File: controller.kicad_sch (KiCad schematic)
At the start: 39 parts, among them U3 STM32F767ZITx, Y1 Crystal

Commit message: Added ESD, updated Footprints, BOM, etc.
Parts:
- removed JP1: SolderJumper_3_Bridged, Jumper:SolderJumper-3_P1.3mm_Bridged12_Pad1.0x1.5mm, symbol Jumper:SolderJumper_3_Bridged12
- removed TP1: UART_RTS, TestPoint:TestPoint_Pad_D1.5mm, symbol Connector:TestPoint
- removed TP1: UART_CTS, TestPoint:TestPoint_Pad_D1.5mm, symbol Connector:TestPoint
- removed Y1: Crystal, TimosFootprints:Crystal_SMD_MicroCrystal_CC6F_T1F_128, symbol Device:Crystal
- added C37, C38: C, Capacitor_SMD:C_0201_0603Metric, symbol Device:C
- added R56: 0R, Resistor_SMD:R_0201_0603Metric, symbol Device:R
- added Y1: CX2016SA25000F0FRZC1, TimosFootprints:CX2016SA25000F0FRZC1, symbol Device:Crystal_GND24
- C3: value 0.1u -> 100n
- D1: value OPTION_LED_1 -> SML-LX0402USBC-TR
- D1: value OPTION_LED_2 -> SML-LX0402USBC-TR
- SW_RESET: value SW_Push -> PTS645SM43SMTR92 LFS
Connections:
- net +3.3V: now also R30.1, R31.1; no longer R30.2, R31.2
- net GEN_SPI_CLK: now also U3.69 (PB10); no longer U3.126 (PG11)
- net GEN_SPI_CSEL: now also U3.28 (PC2); no longer U3.128 (PG13)
- net GEN_SPI_DATA: now also U3.27 (PC1)
- net GND: now also C37.2, C38.2, Y1.2, Y1.4
- net GPIO_BTN_1: now also U3.128 (PG13); no longer U3.90 (PG5)
- net GPIO_BTN_2: now also U3.127 (PG12); no longer U3.89 (PG4)
- net GPIO_LED_1: now also U3.126 (PG11); no longer U3.88 (PG3)
- net GPIO_LED_2: now also U3.125 (PG10); no longer U3.87 (PG2)
- net GPIO_LED_2_JUNCTION: now reaches D1.2 (A), R11.1
- net MCU_VDDUSB: now reaches U3.95 (VDDUSB)
- net MCU_VDDUSB: now also R31.2; no longer R31.1
- net GPIO_LED_1_JUNCTION: now reaches D1.2 (A), R11.1
- net MCU_PDR_ON: now reaches R29.2, U3.143 (PDR_ON)
- net MCU_VDDSDMMC: now reaches U3.121 (VDDSDMMC)
- net MCU_VDDSDMMC: now also R30.2; no longer R30.1
- net JTAG_TMS: now reaches U3.105 (PA13)
- net JTAG_TCK: now reaches U3.109 (PA14)
- net JTAG_TDI: now reaches U3.110 (PA15)
- net JTAG_TDO: now reaches U3.133 (PB3)
- net JTAG_NTRST: now reaches U3.134 (PB4)
- net MCU_BOOT0: now reaches R27.1, SW_BOOT1.2, U3.138 (BOOT0)
- net MCU_VBAT: now reaches R12.2, U3.6 (VBAT)
- net CRYSTAL_PH0 renamed MCU_CRYSTAL_PH0
- net MCU_CRYSTAL_PH0: now also C38.1, Y1.1
- net CRYSTAL_PH1 renamed MCU_CRYSTAL_PH1
- net MCU_CRYSTAL_PH1: now also R56.2
- net GEN_SPI_DATA_MCU_0: no longer names the net of U3.43 (PA7)
- net GEN_SPI_DATA_MCU_1: no longer names the net of U3.135 (PB5)
- net GLOBAL_NRESET renamed JTAG_NSRST
- new net MCU_CRYSTAL_3: C37.1, R56.1, Y1.3
- no-connect marks 93 -> 89
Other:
- note added: "TODO: Cs + R dimensionieren"
- note added: "TODO: Schalter heraussuchen"
- note removed: "If there is a problem with a timer and an SPI output pin, use this jumper to select the correct SPI output on the MCU."
- note removed: "Sine Generator SPI Data selection"
- note removed: "TODO"
- moved on the sheet: C3, D1, R11, R12, R27, R29, R30, R31, SW_BOOT1, SW_RESET, U3

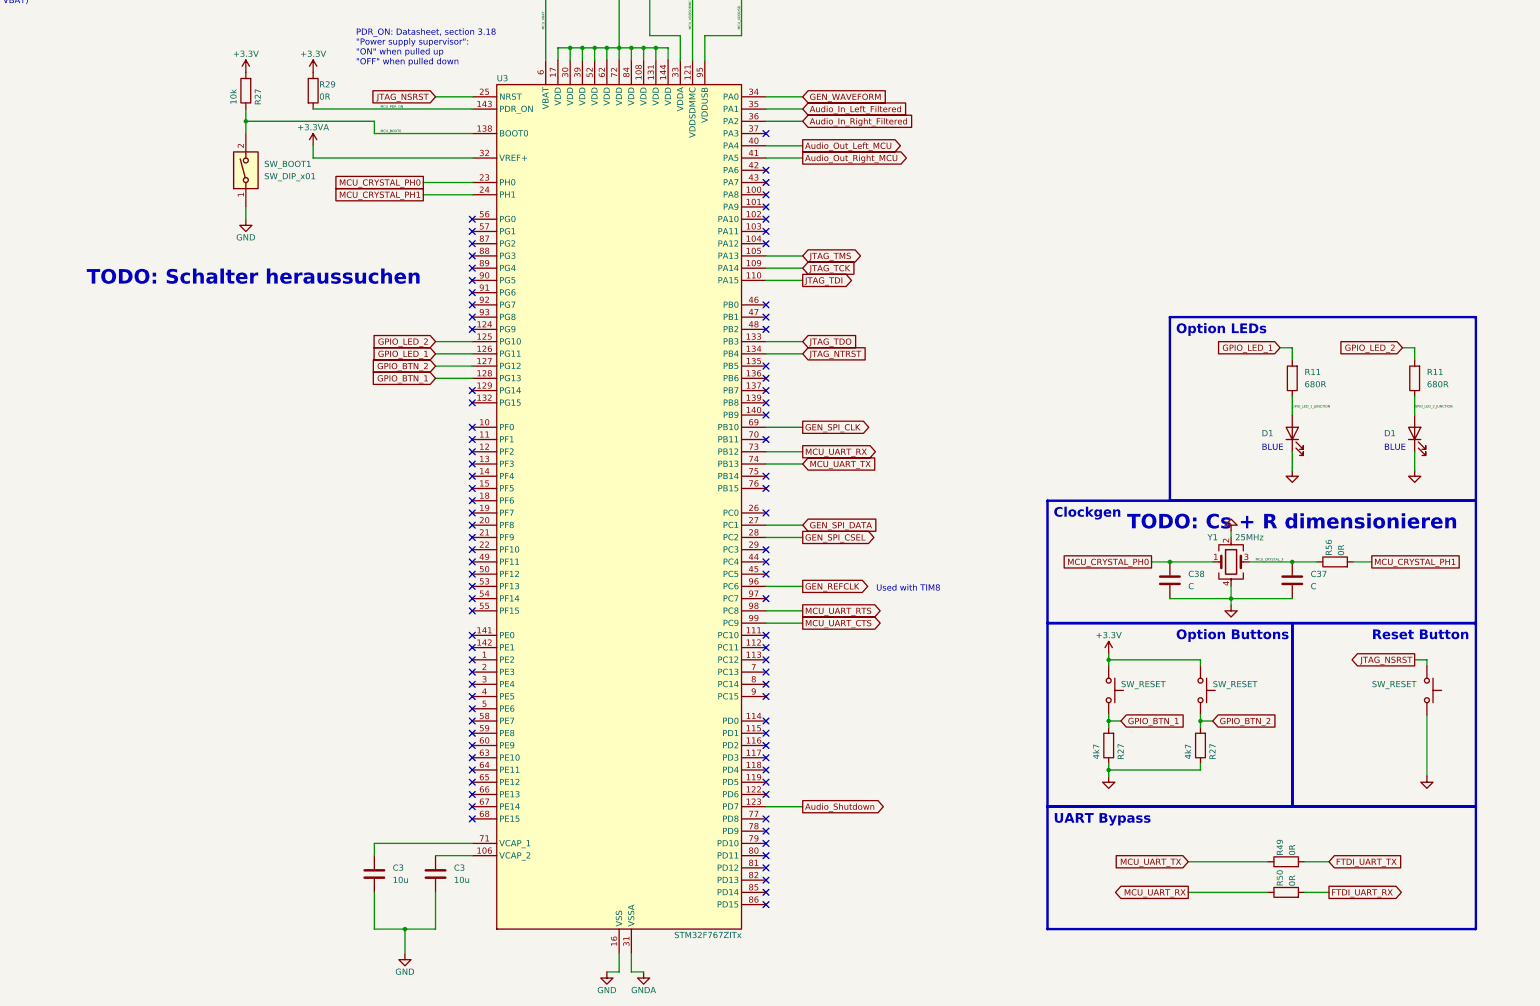
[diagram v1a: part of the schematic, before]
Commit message: Schematic is done for now, starting layout
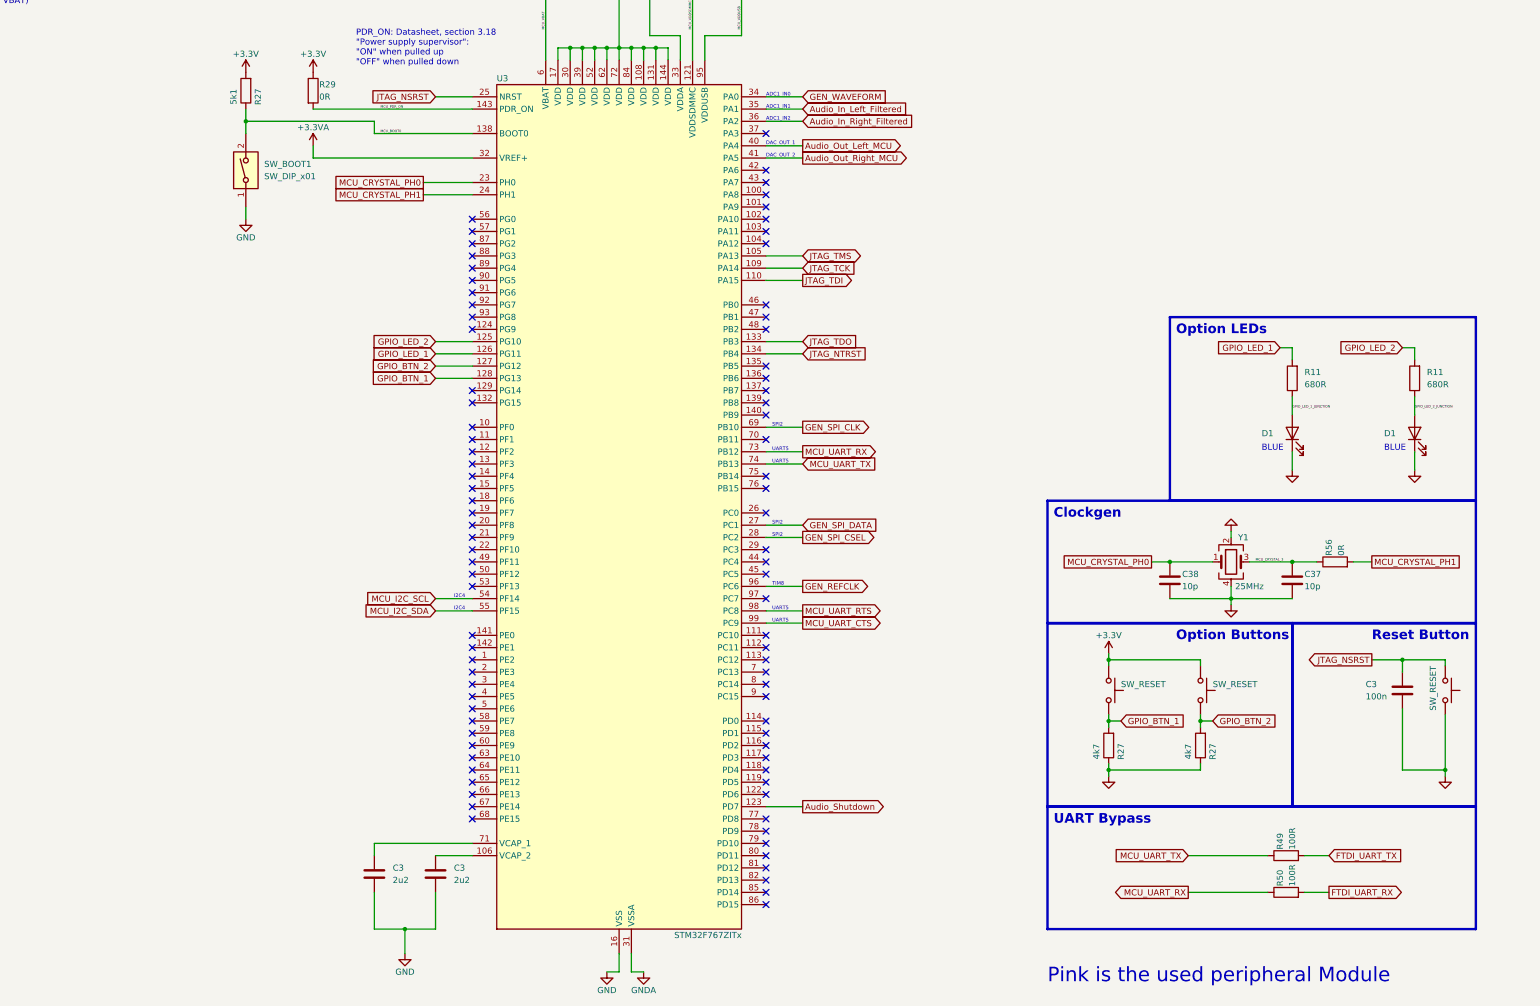
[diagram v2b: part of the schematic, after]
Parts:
- added C3: 100n, Capacitor_SMD:C_0603_1608Metric, symbol Device:C
- C3: value 10u -> 2u2
- C37, C38: value C -> 10p
- D1: Distributor Link (none) -> https://www.mouser.de/ProductDetail/Lumex/SML-LX0402USBC-TR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; MFN SML-LX0402USBC-TR -> (none); Manufacturer (none) -> Lumex; Manufacturer Number (none) -> SML-LX0402USBC-TR
- R27: value 10k -> 5k1
- R49, R50: value 0R -> 100R
- SW_BOOT1: footprint Button_Switch_THT:SW_DIP_SPSTx01_Slide_9.78x4.72mm_W7.62mm_P2.54mm -> TimosFootprints:DS01-254-L-01BE; Distributor Link (none) -> https://www.mouser.de/ProductDetail/CUI-Devices/DS01-254-L-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; Manufacturer (none) -> CUI Devices; Manufacturer Number (none) -> DS01-254-L-01BE
- SW_RESET: Distributor Link (none) -> https://www.mouser.de/ProductDetail/CK/PTS645SM43SMTR92LFS?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; MFN PTS645SM43SMTR92 LFS -> (none); Manufacturer (none) -> C&K; Manufacturer Number (none) -> PTS645SM43SMTR92 LFS
- U3: Distributor Link (none) -> https://www.mouser.de/ProductDetail/STMicroelectronics/STM3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; Manufacturer (none) -> STMicroelectronics; Manufacturer Number (none) -> STM32F767ZIT6
- Y1: value CX2016SA25000F0FRZC1 -> 25MHz; footprint TimosFootprints:CX2016SA25000F0FRZC1 -> Crystal:Crystal_SMD_2016-4Pin_2.0x1.6mm; Distributor Link (none) -> https://www.mouser.de/ProductDetail/KYOCERA-AVX/CX2016SA250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; Frequenz 25MHz -> (none); MFN CX2016SA25000F0FRZC1 -> (none); Manufacturer (none) -> KYOCERA AVX; Manufacturer Number (none) -> CX2016SA25000F0FRZC1
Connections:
- net GND: now also C3.2
- net JTAG_NSRST: now also C3.1
- net MCU_I2C_SCL: now reaches U3.54 (PF14)
- net MCU_I2C_SDA: now reaches U3.55 (PF15)
- no-connect marks 89 -> 87
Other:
- note added: "ADC1_IN0"
- note added: "ADC1_IN1"
- note added: "ADC1_IN2"
- note added: "DAC_OUT_1"
- note added: "DAC_OUT_2"
- note added: "I2C4"
- note added: "Pink is the used peripheral Module"
- note added: "SPI2"
- note added: "TIM8"
- note added: "UART5"
- note removed: "TODO: Cs + R dimensionieren"
- note removed: "TODO: Schalter heraussuchen"
- note removed: "Used with TIM8"
- moved on the sheet: R49, SW_RESET

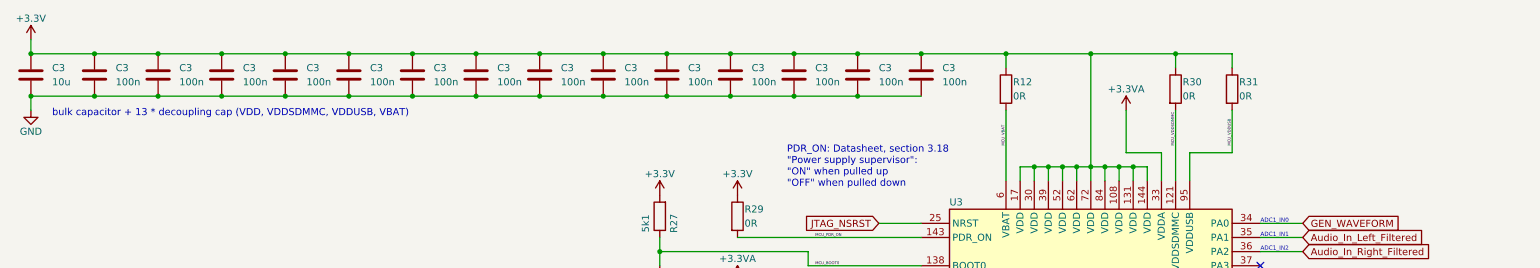
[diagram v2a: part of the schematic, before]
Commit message: Layout done, footprints mostly assigned, 3D models assigned if not annoying to get. Few TODOs left and they are marked on the PCB.
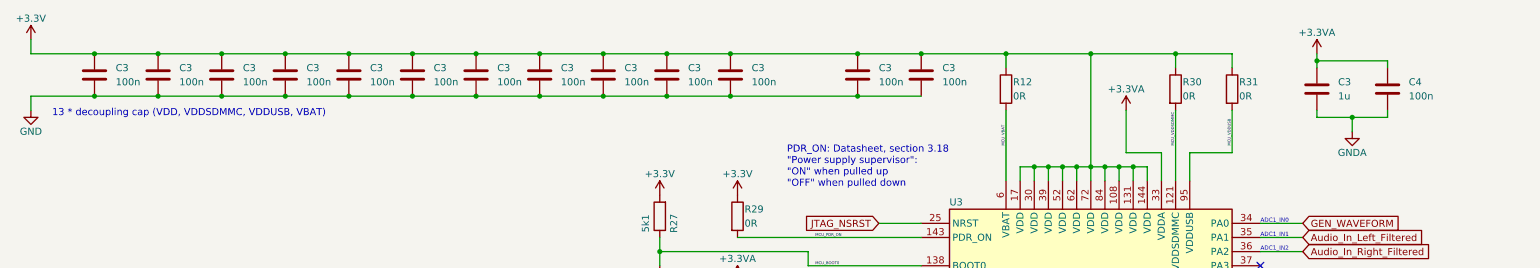
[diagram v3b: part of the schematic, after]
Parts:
- removed C3: 10u, Capacitor_SMD:C_0603_1608Metric, symbol Device:C
- removed C3: 100n, Capacitor_SMD:C_0603_1608Metric, symbol Device:C
- added C3: 1u, Capacitor_SMD:C_0603_1608Metric, symbol Device:C
- added C4: 100n, Capacitor_SMD:C_0603_1608Metric, symbol Device:C
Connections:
- net +3.3VA: now also C3.1, C4.1
- net GNDA: now also C3.2, C4.2
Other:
- note added: "13 * decoupling cap (VDD, VDDSDMMC, VDDUSB, VBAT)"
- note removed: "bulk capacitor + 13 * decoupling cap (VDD, VDDSDMMC, VDDUSB, VBAT)"

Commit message: Board outline finished, component placement, added markers, added annotations, etc.
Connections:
- net GPIO_OPT_0: now reaches U3.65 (PE12)
- net GPIO_OPT_1: now reaches U3.66 (PE13)
- net GPIO_OPT_2: now reaches U3.67 (PE14)
- net GPIO_OPT_3: now reaches U3.68 (PE15)
- no-connect marks 87 -> 83
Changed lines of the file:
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@@
   )
   (no_connect (at 185.42 157.48))
-  (no_connect (at 185.42 210.82))
   (no_connect (at 185.42 167.64))
   (no_connect (at 246.38 218.44))
@@
   (no_connect (at 246.38 127))
   (no_connect (at 185.42 170.18))
-  (no_connect (at 185.42 218.44))
   (no_connect (at 246.38 205.74))
   (no_connect (at 185.42 195.58))
@@
   (no_connect (at 246.38 180.34))
   (no_connect (at 246.38 165.1))
-  (no_connect (at 185.42 215.9))
   (no_connect (at 185.42 193.04))
   (no_connect (at 246.38 220.98))
@@
   (no_connect (at 246.38 124.46))
   (no_connect (at 246.38 200.66))
-  (no_connect (at 185.42 213.36))
   (no_connect (at 185.42 185.42))
   (no_connect (at 246.38 132.08))
@@
     (stroke (width 0) (type default))
   )
+  (wire (pts (xy 177.8 215.9) (xy 185.42 215.9))
+    (stroke (width 0) (type default))
+  )
   (wire (pts (xy 246.38 144.78) (xy 254 144.78))
     (stroke (width 0) (type default))
@@
     (stroke (width 0) (type default))
   )
+  (wire (pts (xy 177.8 210.82) (xy 185.42 210.82))
+    (stroke (width 0) (type default))
+  )
   (wire (pts (xy 246.38 160.02) (xy 254 160.02))
     (stroke (width 0) (type default))
@@
     (stroke (width 0) (type default))
   )
+  (wire (pts (xy 177.8 213.36) (xy 185.42 213.36))
+    (stroke (width 0) (type default))
+  )
   (wire (pts (xy 233.68 55.88) (xy 233.68 60.96))
     (stroke (width 0) (type default))
@@
   )
   (wire (pts (xy 205.74 58.42) (xy 205.74 60.96))
+    (stroke (width 0) (type default))
+  )
+  (wire (pts (xy 177.8 218.44) (xy 185.42 218.44))
     (stroke (width 0) (type default))
   )
@@
     )
   )
+  (global_label "GPIO_OPT_2" (shape bidirectional) (at 177.8 215.9 180) (fields_autoplaced)
+    (effects (font (size 1.27 1.27)) (justify right))
+    (property "Intersheetrefs" "${INTERSHEET_REFS}" (at 162.5154 215.9 0)
+      (effects (font (size 1.27 1.27)) (justify right) hide)
+    )
+  )
+  (global_label "GPIO_OPT_3" (shape bidirectional) (at 177.8 218.44 180) (fields_autoplaced)
+    (effects (font (size 1.27 1.27)) (justify right))
+    (property "Intersheetrefs" "${INTERSHEET_REFS}" (at 162.5154 218.44 0)
+      (effects (font (size 1.27 1.27)) (justify right) hide)
+    )
+  )
   (global_label "GEN_REFCLK" (shape output) (at 254 170.18 0) (fields_autoplaced)
     (effects (font (size 1.27 1.27)) (justify left))
@@
     )
   )
+  (global_label "GPIO_OPT_0" (shape bidirectional) (at 177.8 210.82 180) (fields_autoplaced)
+    (effects (font (size 1.27 1.27)) (justify right))
+    (property "Intersheetrefs" "${INTERSHEET_REFS}" (at 162.5154 210.82 0)
+      (effects (font (size 1.27 1.27)) (justify right) hide)
+    )
+  )
   (global_label "MCU_CRYSTAL_PH0" (shape passive) (at 175.26 86.36 180) (fields_autoplaced)
     (effects (font (size 1.27 1.27)) (justify right))
@@
     )
   )
+  (global_label "GPIO_OPT_1" (shape bidirectional) (at 177.8 213.36 180) (fields_autoplaced)
+    (effects (font (size 1.27 1.27)) (justify right))
+    (property "Intersheetrefs" "${INTERSHEET_REFS}" (at 162.5154 213.36 0)
+      (effects (font (size 1.27 1.27)) (justify right) hide)
+    )
+  )
